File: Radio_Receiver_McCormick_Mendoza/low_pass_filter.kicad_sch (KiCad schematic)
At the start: 0 parts

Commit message: Merge conflict resolution.
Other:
- title: (none) -> Radio Receiver
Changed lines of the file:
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@@
 	(paper "A4")
 	(title_block
+		(title "Radio Receiver")
 		(date "2026-04-19")
 		(rev "0.0.1")

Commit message: Propogated Title Block Fields
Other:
- company: (none) -> Walla Walla University
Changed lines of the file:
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@@
 		(date "2026-04-19")
 		(rev "0.0.1")
+		(company "Walla Walla University")
 		(comment 2 "Daniel Mendoza")
 		(comment 3 "Jeffrey McCormick")

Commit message: Added Daniel Mendoza's changes to KiCAD files.
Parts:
- added C12, C13: 4.7n, symbol Device:C
- added C14, C15: 10n, symbol Device:C
- added C16: 0.1u, symbol Device:C
- added C19, C20: 10u, symbol Device:C
- added R11, R12, R13, R14: 1.1k, symbol Device:R
- added R15, R16: 100, symbol Device:R
- added U10: OPA1662DGK, Package_SO:VSSOP-8_3x3mm_P0.65mm, symbol Amplifier_Operational:OPA1662DGK
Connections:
- new net: C19.2, R15.1
- new net: C15.1, R13.2, U10.3 (+)
- new net: C13.1, R12.2, R14.1
- new net: C12.2, R11.2, R13.1
- new net: C20.2, R16.1
- new net: C12.1, C19.1, U10.1, U10.2 (-)
- new net: C13.2, C20.1, U10.6 (-), U10.7
- new net: C14.2, R14.2, U10.5 (+)
- new net GND: C14.1, C15.2, C16.2, U10.4 (V-)
- new net I Signal: R15.2
- new net I_OUT: R11.1
- new net Q Signal: R16.2
- new net Q_OUT: R12.1
- new net VDDA: U10.8 (V+)

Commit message: Added switchable antenna filters and photos.
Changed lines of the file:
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@@
 	)
 	(global_label "I Signal"
-		(shape input)
+		(shape output)
 		(at 191.77 93.98 0)
 		(fields_autoplaced yes)

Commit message: Added footprints
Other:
- note added: "Verify that the I and Q stay phase-accurate as it approaches the cutoff frequency."
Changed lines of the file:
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@@
 		(comment 3 "Jeffrey McCormick")
+	)
+	(text "Verify that the I and Q stay phase-accurate\nas it approaches the cutoff frequency. "
+		(exclude_from_sim no)
+		(at 77.216 41.656 0)
+		(effects
+			(font
+				(size 1.27 1.27)
+			)
+		)
 	)
 	(junction

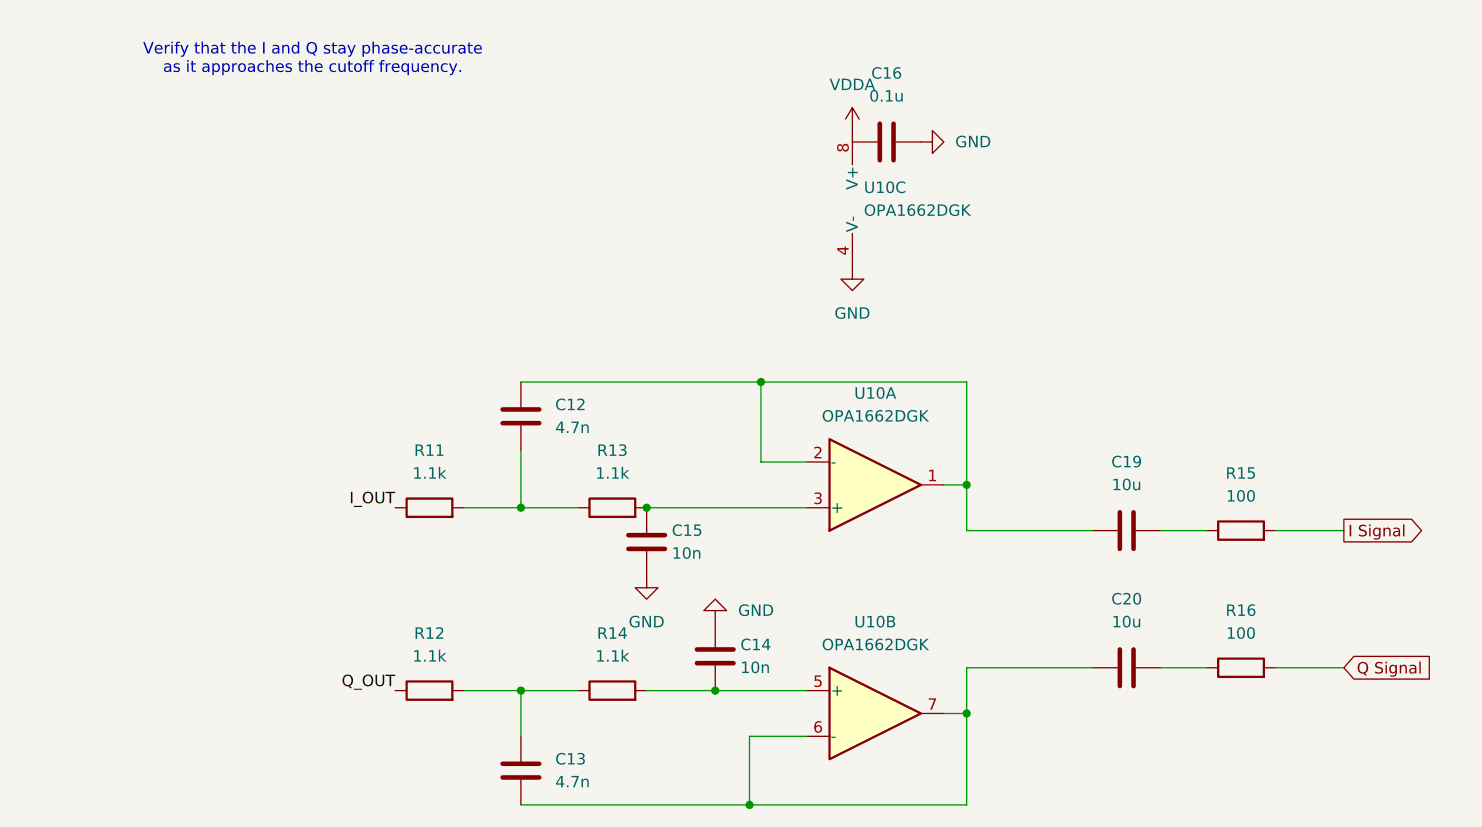
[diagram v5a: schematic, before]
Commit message: Schematic connection edits
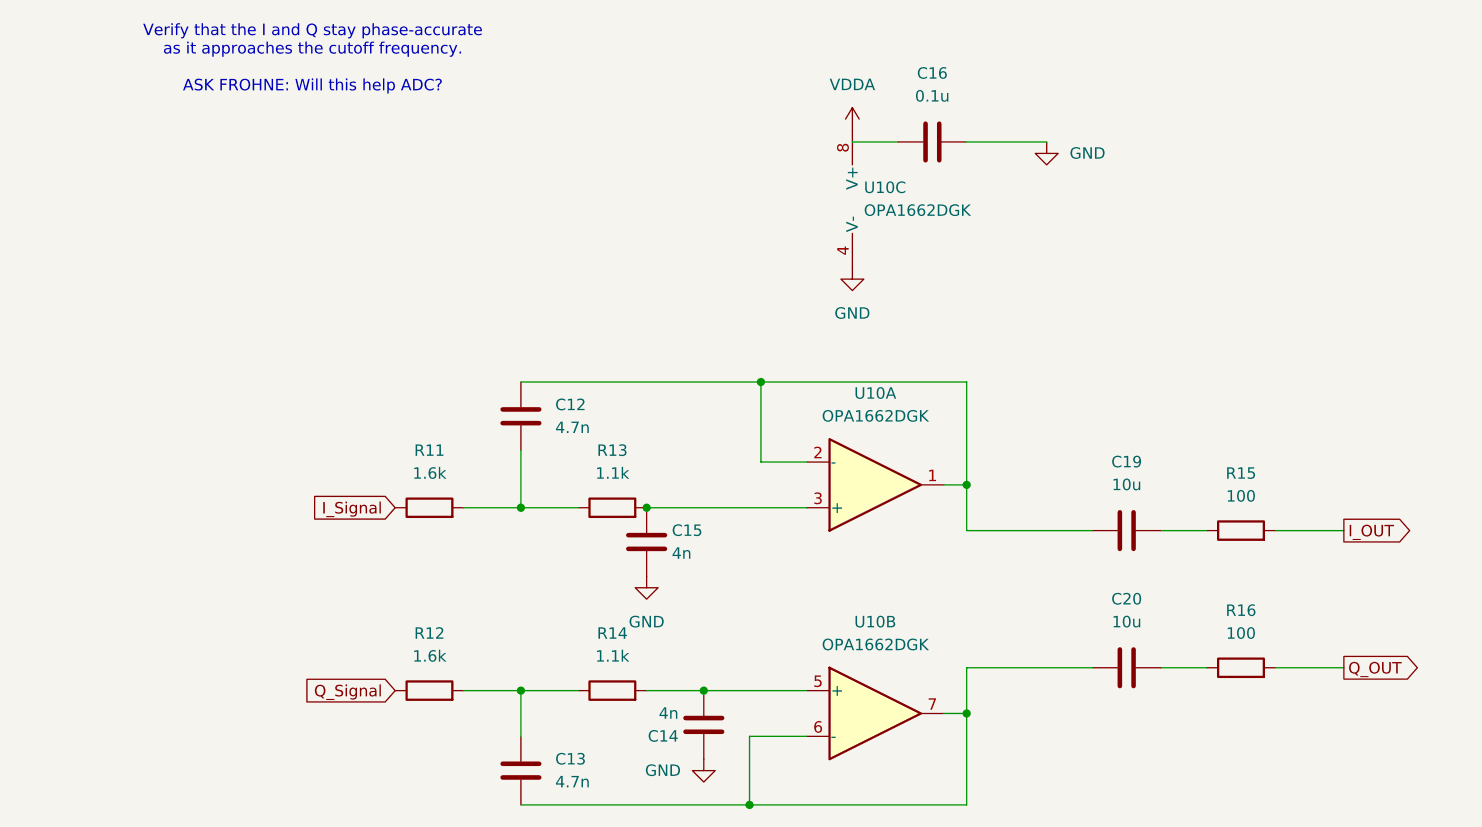
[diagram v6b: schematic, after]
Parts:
- C14, C15: value 10n -> 4n
- R11, R12: value 1.1k -> 1.6k
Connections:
- net I Signal is gone; now on net I_OUT: R15.2
- net Q Signal is gone; now on net Q_OUT: R16.2
- net I_OUT: no longer R11.1
- net Q_OUT: no longer R12.1
- new net I_Signal: R11.1
- new net Q_Signal: R12.1
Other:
- note added: "Verify that the I and Q stay phase-accurate as it approaches the cutoff frequency. ASK FROHNE: Will this help ADC?"
- note removed: "Verify that the I and Q stay phase-accurate as it approaches the cutoff frequency."
- moved on the sheet: C14, C16
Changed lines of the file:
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@@
 		(comment 3 "Jeffrey McCormick")
 	)
-	(text "Verify that the I and Q stay phase-accurate\nas it approaches the cutoff frequency. "
+	(text "Verify that the I and Q stay phase-accurate\nas it approaches the cutoff frequency. \n\nASK FROHNE: Will this help ADC?"
 		(exclude_from_sim no)
 		(at 77.216 41.656 0)
@@
 	)
 	(junction
+		(at 120.65 111.76)
+		(diameter 0)
+		(color 0 0 0 0)
+	)
+	(junction
 		(at 149.86 88.9)
 		(diameter 0)
@@
 	)
 	(junction
-		(at 121.92 111.76)
-		(diameter 0)
-		(color 0 0 0 0)
-	)
-	(junction
 		(at 125.73 124.46)
 		(diameter 0)
@@
 	(wire
 		(pts
-			(xy 114.3 111.76) (xy 121.92 111.76)
+			(xy 114.3 111.76) (xy 120.65 111.76)
 		)
 		(stroke
@@
 	(wire
 		(pts
+			(xy 137.16 50.8) (xy 142.24 50.8)
+		)
+		(stroke
+			(width 0)
+			(type default)
+		)
+	)
+	(wire
+		(pts
 			(xy 184.15 109.22) (xy 191.77 109.22)
 		)
@@
 	(wire
 		(pts
+			(xy 120.65 111.76) (xy 132.08 111.76)
+		)
+		(stroke
+			(width 0)
+			(type default)
+		)
+	)
+	(wire
+		(pts
 			(xy 149.86 114.3) (xy 149.86 124.46)
 		)
@@
 	(wire
 		(pts
+			(xy 158.75 50.8) (xy 149.86 50.8)
+		)
+		(stroke
+			(width 0)
+			(type default)
+		)
+	)
+	(wire
+		(pts
 			(xy 132.08 86.36) (xy 127 86.36)
 		)
@@
 		)
 	)
-	(wire
-		(pts
-			(xy 121.92 111.76) (xy 132.08 111.76)
-		)
-		(stroke
-			(width 0)
-			(type default)
-		)
-	)
-	(label "I_OUT"
-		(at 86.36 91.44 180)
+	(global_label "I_OUT"
+		(shape output)
+		(at 191.77 93.98 0)
+		(fields_autoplaced yes)
 		(effects
 			(font
 				(size 1.27 1.27)
 			)
-			(justify right bottom)
-		)
-	)
-	(label "Q_OUT"
-		(at 86.36 111.76 180)
+			(justify left)
+		)
+		(property "Intersheetrefs" "${INTERSHEET_REFS}"
+			(at 199.9562 93.98 0)
+			(hide yes)
+			(show_name no)
+			(do_not_autoplace no)
+			(effects
+				(font
+					(size 1.27 1.27)
+				)
+				(justify left)
+			)
+		)
+	)
+	(global_label "I_Signal"
+		(shape input)
+		(at 86.36 91.44 180)
+		(fields_autoplaced yes)
 		(effects
 			(font
 				(size 1.27 1.27)
 			)
-			(justify right bottom)
-		)
-	)
-	(global_label "I Signal"
-		(shape output)
-		(at 191.77 93.98 0)
+			(justify right)
+		)
+		(property "Intersheetrefs" "${INTERSHEET_REFS}"
+			(at 75.8759 91.44 0)
+			(hide yes)
+			(show_name no)
+			(do_not_autoplace no)
+			(effects
+				(font
+					(size 1.27 1.27)
+				)
+				(justify right)
+			)
+		)
+	)
+	(global_label "Q_Signal"
+		(shape input)
+		(at 86.36 111.76 180)
 		(fields_autoplaced yes)
 		(effects
@@
 				(size 1.27 1.27)
 			)
-			(justify left)
+			(justify right)
 		)
 		(property "Intersheetrefs" "${INTERSHEET_REFS}"
-			(at 202.2541 93.98 0)
-			(hide yes)
-			(show_name no)
-			(do_not_autoplace no)
-			(effects
-				(font
-					(size 1.27 1.27)
-				)
-				(justify left)
-			)
-		)
-	)
-	(global_label "Q Signal"
-		(shape input)
+			(at 75.1502 111.76 0)
+			(hide yes)
+			(show_name no)
+			(do_not_autoplace no)
+			(effects
+				(font
+					(size 1.27 1.27)
+				)
+				(justify right)
+			)
+		)
+	)
+	(global_label "Q_OUT"
+		(shape output)
 		(at 191.77 109.22 0)
 		(fields_autoplaced yes)
@@
 		)
 		(property "Intersheetrefs" "${INTERSHEET_REFS}"
-			(at 202.9798 109.22 0)
+			(at 200.6819 109.22 0)
 			(hide yes)
 			(show_name no)
@@
 			)
 		)
-		(property "Value" "10n"
+		(property "Value" "4n"
 			(at 117.094 96.52 0)
 			(show_name no)
@@
 			)
 		)
-		(property "Value" "1.1k"
+		(property "Value" "1.6k"
 			(at 90.17 107.95 90)
 			(show_name no)
@@
 			)
 		)
-		(property "Value" "1.1k"
+		(property "Value" "1.6k"
 			(at 90.17 87.63 90)
 			(show_name no)
@@
 	(symbol
 		(lib_id "power:GND")
-		(at 121.92 104.14 180)
+		(at 120.65 119.38 0)
 		(unit 1)
 		(body_style 1)
@@
 		(fields_autoplaced yes)
 		(property "Reference" "#PWR033"
-			(at 121.92 97.79 0)
+			(at 120.65 125.73 0)
 			(hide yes)
 			(show_name no)
@@
 		)
 		(property "Value" "GND"
-			(at 124.46 102.8699 0)
+			(at 118.11 120.6501 0)
 			(show_name no)
 			(do_not_autoplace no)
@@
 		)
 		(property "Footprint" ""
-			(at 121.92 104.14 0)
+			(at 120.65 119.38 0)
 			(hide yes)
 			(show_name no)
@@
 		)
 		(property "Datasheet" ""
-			(at 121.92 104.14 0)
+			(at 120.65 119.38 0)
 			(hide yes)
 			(show_name no)
@@
 		)
 		(property "Description" "Power symbol creates a global label with name \"GND\" , ground"
-			(at 121.92 104.14 0)
+			(at 120.65 119.38 0)
 			(hide yes)
 			(show_name no)
@@
 	(symbol
 		(lib_id "Device:C")
-		(at 140.97 50.8 90)
+		(at 146.05 50.8 90)
 		(unit 1)
 		(body_style 1)
@@
 		(fields_autoplaced yes)
 		(property "Reference" "C16"
-			(at 140.97 43.18 90)
+			(at 146.05 43.18 90)
 			(show_name no)
 			(do_not_autoplace no)
@@
 		)
 		(property "Value" "0.1u"
-			(at 140.97 45.72 90)
+			(at 146.05 45.72 90)
 			(show_name no)
 			(do_not_autoplace no)
@@
 		)
 		(property "Footprint" ""
-			(at 144.78 49.8348 0)
+			(at 149.86 49.8348 0)
 			(hide yes)
 			(show_name no)
@@
 		)
 		(property "Datasheet" ""
-			(at 140.97 50.8 0)
+			(at 146.05 50.8 0)
 			(hide yes)
 			(show_name no)
@@
 		)
 		(property "Description" "Unpolarized capacitor"
-			(at 140.97 50.8 0)
+			(at 146.05 50.8 0)
 			(hide yes)
 			(show_name no)
@@
 	(symbol
 		(lib_id "Device:C")
-		(at 121.92 107.95 0)
+		(at 120.65 115.57 180)
 		(unit 1)
 		(body_style 1)
@@
 		(dnp no)
 		(property "Reference" "C14"
-			(at 124.714 106.68 0)
+			(at 117.856 116.84 0)
 			(show_name no)
 			(do_not_autoplace no)
@@
 			)
 		)
-		(property "Value" "10n"
-			(at 124.714 109.22 0)
+		(property "Value" "4n"
+			(at 117.856 114.3 0)
 			(show_name no)
 			(do_not_autoplace no)
@@
 		)
 		(property "Footprint" ""
-			(at 122.8852 111.76 0)
+			(at 119.6848 111.76 0)
 			(hide yes)
 			(show_name no)
@@
 		)
 		(property "Datasheet" ""
-			(at 121.92 107.95 0)
+			(at 120.65 115.57 0)
 			(hide yes)
 			(show_name no)
@@
 		)
 		(property "Description" "Unpolarized capacitor"
-			(at 121.92 107.95 0)
+			(at 120.65 115.57 0)
 			(hide yes)
 			(show_name no)
@@
 	(symbol
 		(lib_id "power:GND")
-		(at 144.78 50.8 90)
+		(at 158.75 50.8 0)
 		(unit 1)
 		(body_style 1)
@@
 		(fields_autoplaced yes)
 		(property "Reference" "#PWR036"
-			(at 151.13 50.8 0)
+			(at 158.75 57.15 0)
 			(hide yes)
 			(show_name no)
@@
 		)
 		(property "Value" "GND"
-			(at 148.59 50.7999 90)
-			(show_name no)
-			(do_not_autoplace no)
-			(effects
-				(font
-					(size 1.27 1.27)
-				)
-				(justify right)
+			(at 161.29 52.0699 0)
+			(show_name no)
+			(do_not_autoplace no)
+			(effects
+				(font
+					(size 1.27 1.27)
+				)
+				(justify left)
 			)
 		)
 		(property "Footprint" ""
-			(at 144.78 50.8 0)
+			(at 158.75 50.8 0)
 			(hide yes)
 			(show_name no)
@@
 		)
 		(property "Datasheet" ""
-			(at 144.78 50.8 0)
+			(at 158.75 50.8 0)
 			(hide yes)
 			(show_name no)
@@
 		)
 		(property "Description" "Power symbol creates a global label with name \"GND\" , ground"
-			(at 144.78 50.8 0)
-			(hide yes)
-			(show_name no)
+			(at 158.75 50.8 0)
+			(hide yes)
+			(show_name no)

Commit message: Schematic edits power and signal systems
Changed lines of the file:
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@@
+		)
+	)
+	(polyline
+		(pts
+			(xy 44.45 93.98) (xy 132.715 93.98)
+		)
+		(stroke
+			(width 0)
+			(type default)
 		)
 	)
@@
 		)
 	)
+	(polyline
+		(pts
+			(xy 106.045 49.53) (xy 132.715 49.53)
+		)
+		(stroke
+			(width 0)
+			(type default)
+		)
+	)
 	(wire
 		(pts
@@
 		)
 		(stroke
+			(width 0)
+			(type default)
+		)
+	)
+	(polyline
+		(pts
+			(xy 132.715 49.53) (xy 132.715 93.98)
+		)
+		(stroke
